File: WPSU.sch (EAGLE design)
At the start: 27 parts, among them IC1 XCL103E333CR-G, J1 USB3135-XX-X_REVB, U1 LP38692MP-ADJ/NOPBMP05A-M, U2 VISHAY_SI1869DH-T1-E3VISHAY_S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

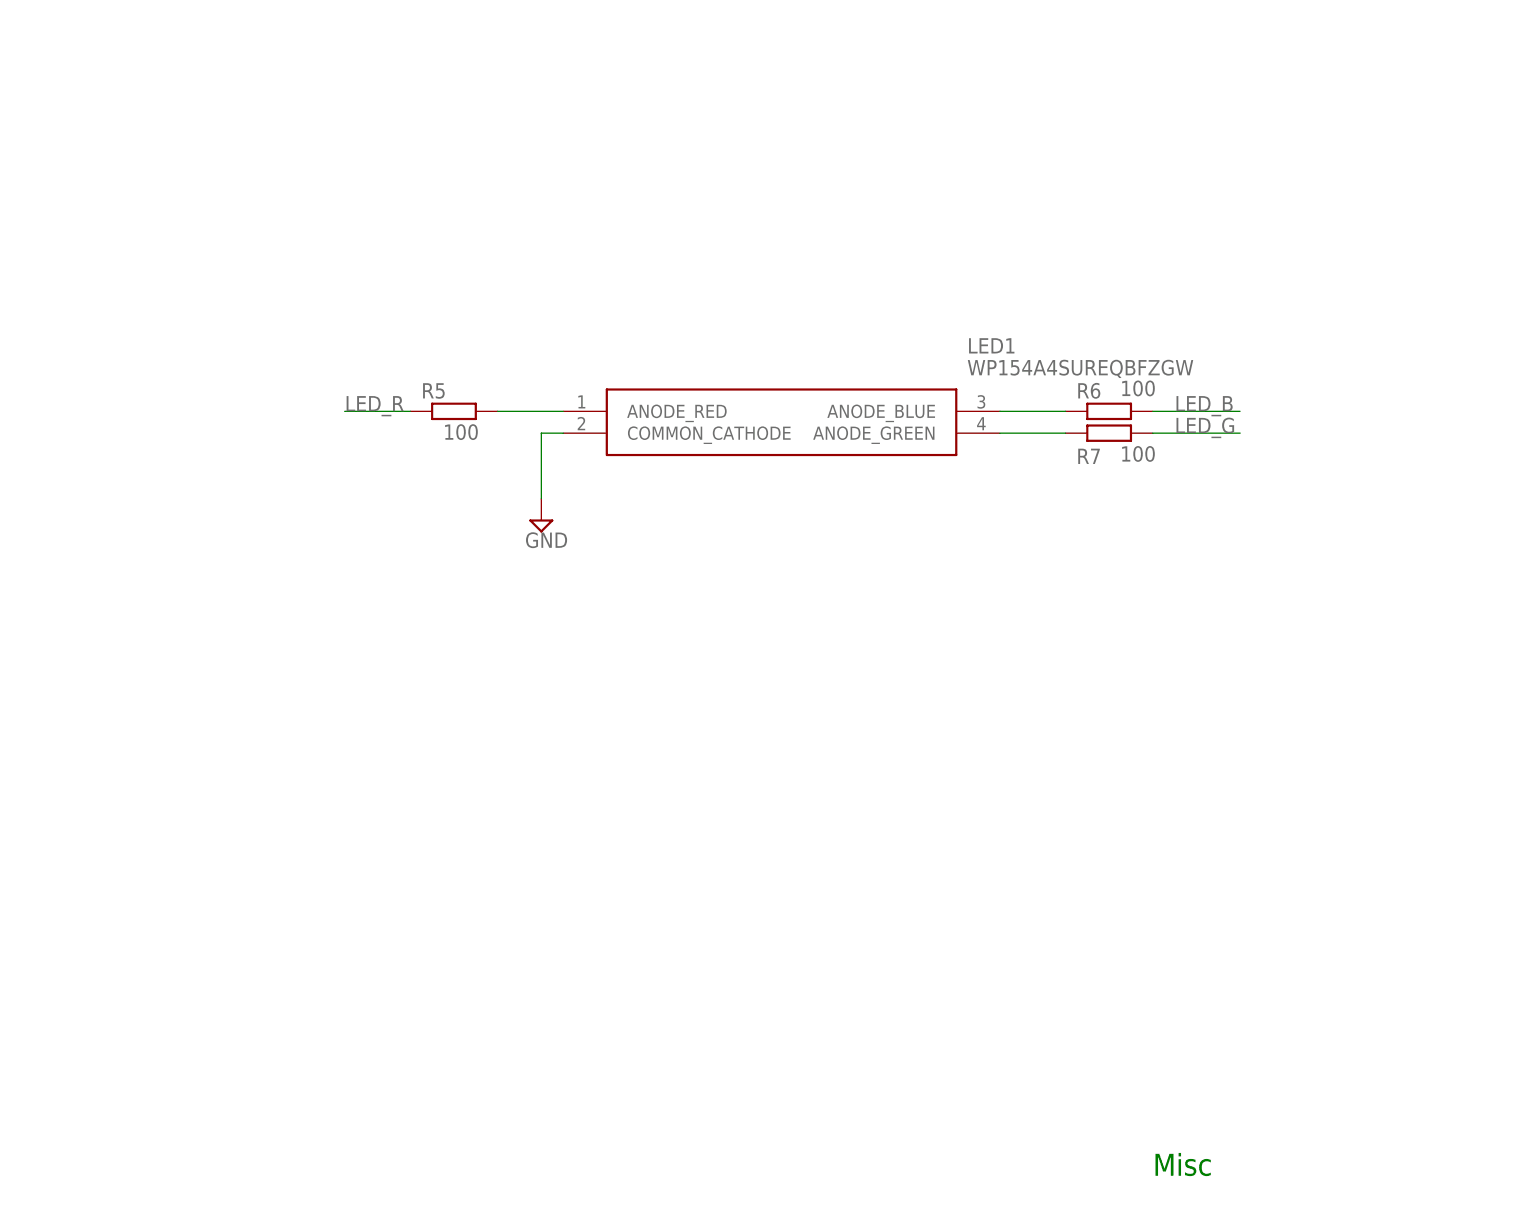
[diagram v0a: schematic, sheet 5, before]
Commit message: Added button and LED drivers
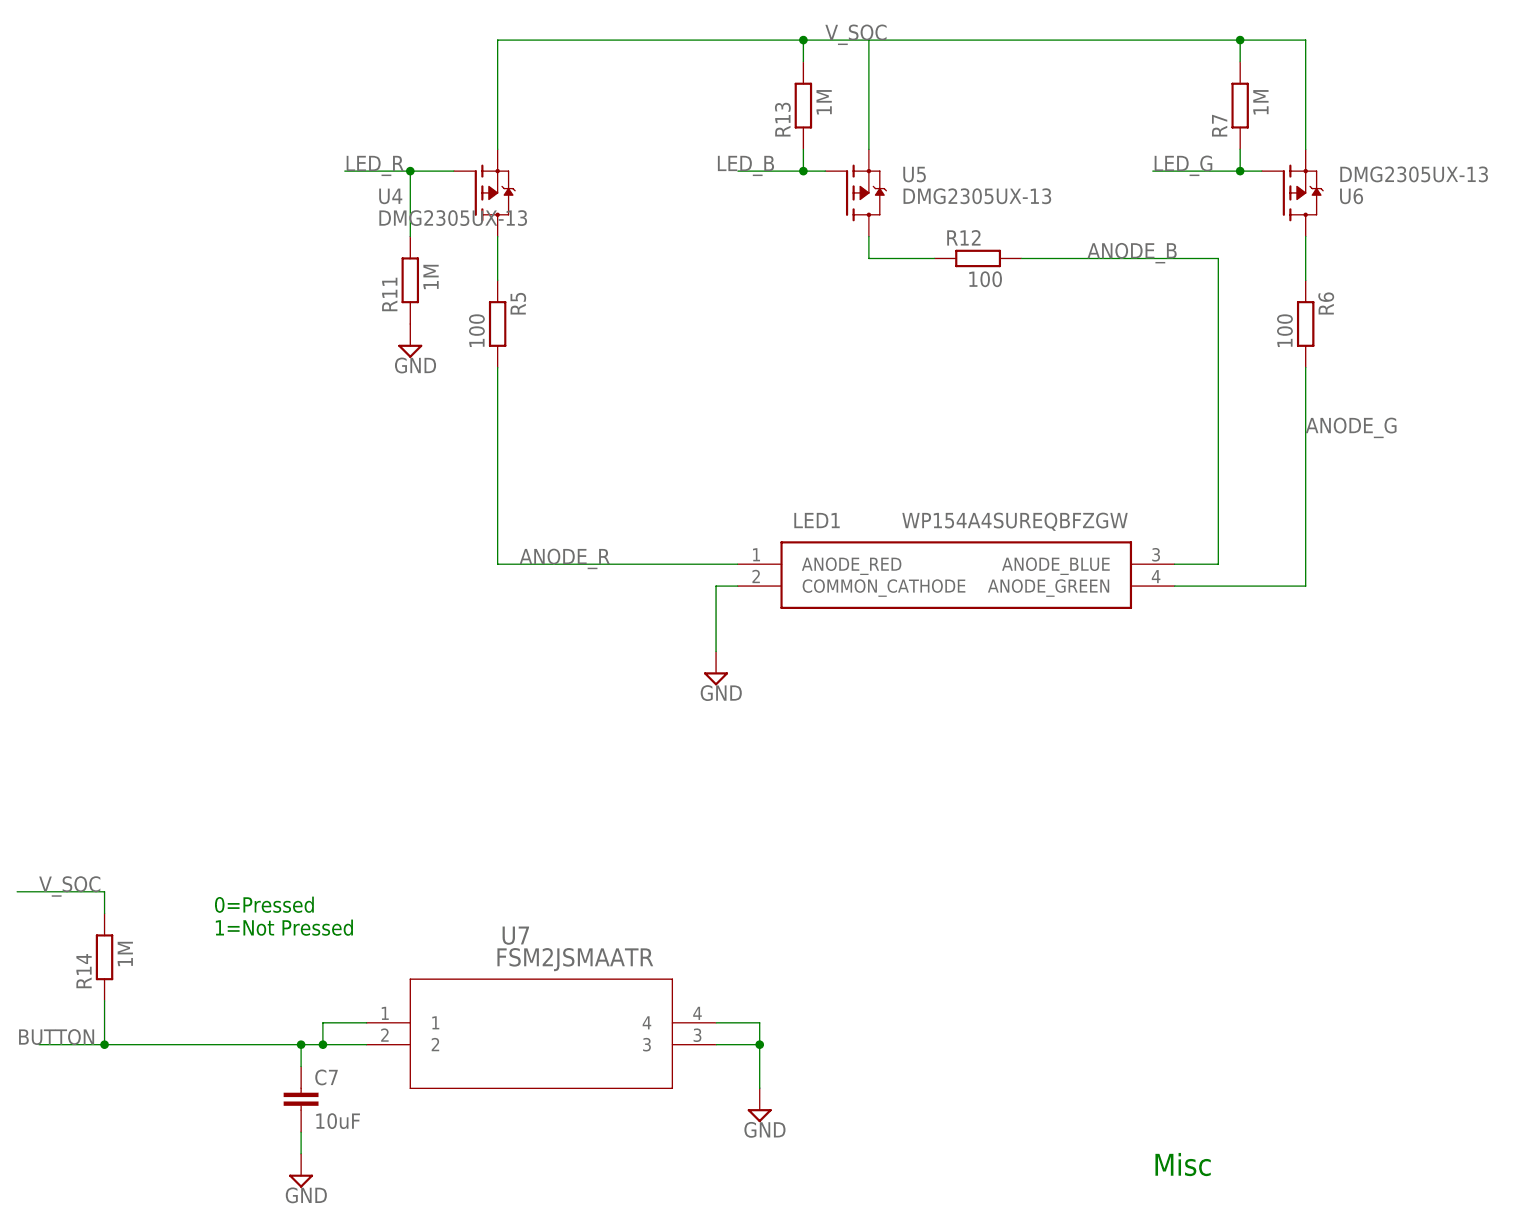
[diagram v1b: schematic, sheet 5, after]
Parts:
- added C5, C6, C7: 10uF, rcl:C-EUC0603
- added R10: 1M, rcl:R-EU_R0603
- added R11, R13, R14: 1M, resistor:R-EU_R0603
- added R12: 100, resistor:R-EU_R0603
- added U3, U4, U5, U6: DMG2305UX-13, custom:DMG2305UX-13
- added U7: FSM2JSMAATR, custom:FSM2JSMAATR
- R7: value 100 -> 1M
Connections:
- net N$6 renamed ANODE_R
- removed net N$11: LED1.ANODE_GREEN, R7.1
- removed net N$17: JP3.2, JP4.2
- new net ANODE_B: LED1.ANODE_BLUE, R12.2
- new net ANODE_G: LED1.ANODE_GREEN, R6.2
- new net BUTTON: C7.1, JP3.2, JP4.2, R14.1, U7.1, U7.2
- new net N$12: R5.1, U4.D
- new net N$14: R12.1, U5.D
- new net N$8: R10.2, U3.G
- new net V_BATT_NO_PROTECT: C5.1, U$1.P1, U3.D
- new net V_BATT_NO_PROTECT1: C6.1
- net GND: now also C5.2, C6.2, C7.2, R10.1, R11.1, U7.3, U7.4
- net LED_B: now also R13.1, U5.G; no longer R6.2
- net LED_G: now also R7.1, U6.G; no longer R7.2
- net LED_R: now also R11.2, U4.G; no longer R5.1
- net N$10: now also U6.D; no longer LED1.ANODE_BLUE
- net V_BATT: now also U3.S; no longer U$1.P1
- net V_SOC: now also R13.2, R14.2, R7.2, U4.S, U5.S, U6.S
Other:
- note added: "0=Pressed 1=Not Pressed"
- note added: "Reverse Polarity Protection"
- moved on the sheet: LED1, R5, R6, R7
